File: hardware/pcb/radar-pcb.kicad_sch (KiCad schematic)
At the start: 49 parts, among them J1 DC 5,5x2,5 mm (+ w srodku), J2 DevKit J1, J3 DevKit J3, J4 HC-SR04 (kabel): VCC TRIG ECH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, J5 Serwo SG90 (kabel): GND +5V S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, J6 MAX7219 Elegoo: VCC GND DIN C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, J7 OLED SH1106: VCC GND SCK SDA, J8 Buzzer: + -, J9 Przycisk zewnetrzny, Q1 AO3401A (P-MOSFET), Q2 MMBT3904, SW1 Przycisk ON/standby (katowy), U1 SN74AHCT125N

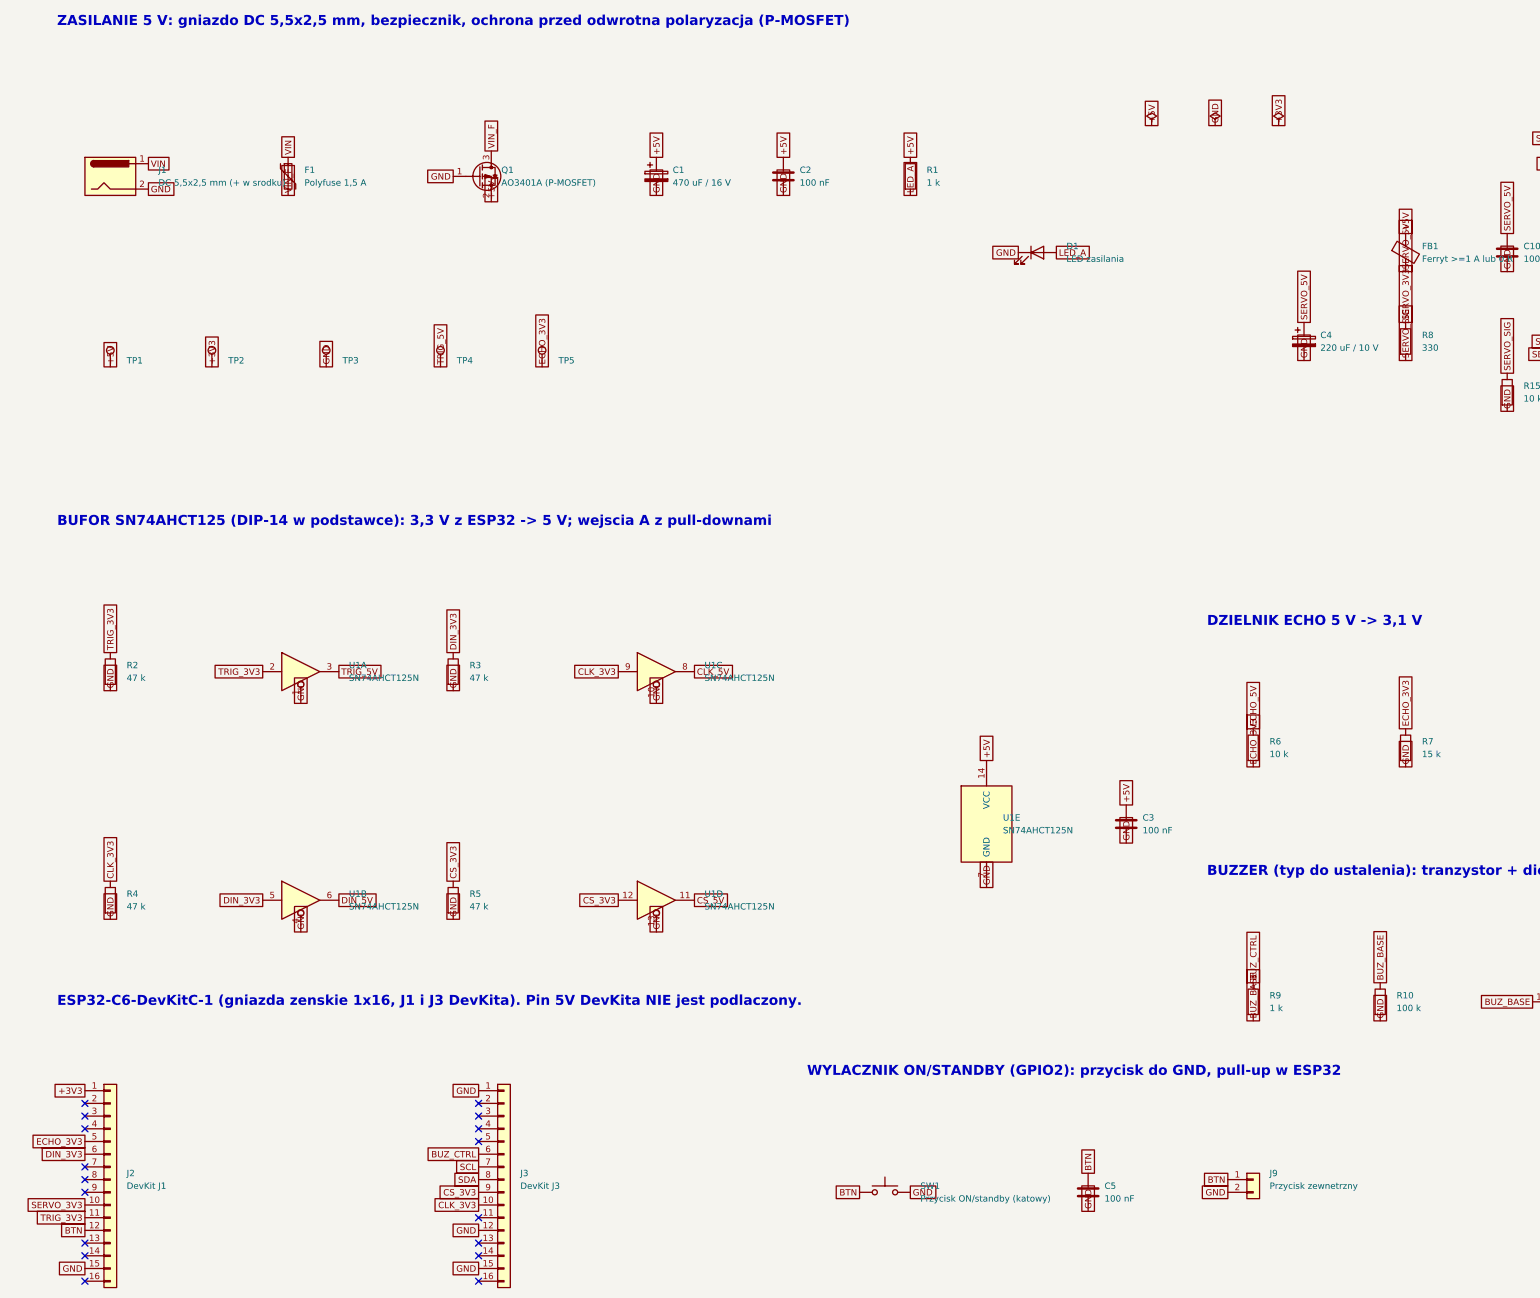
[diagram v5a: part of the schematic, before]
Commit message: PCB: USB-C power input replaces DC jack; DevKit 5V pin tied to board 5V
Co-Authored-By: Claude Sonnet 5.5 <noreply@anthropic.com>
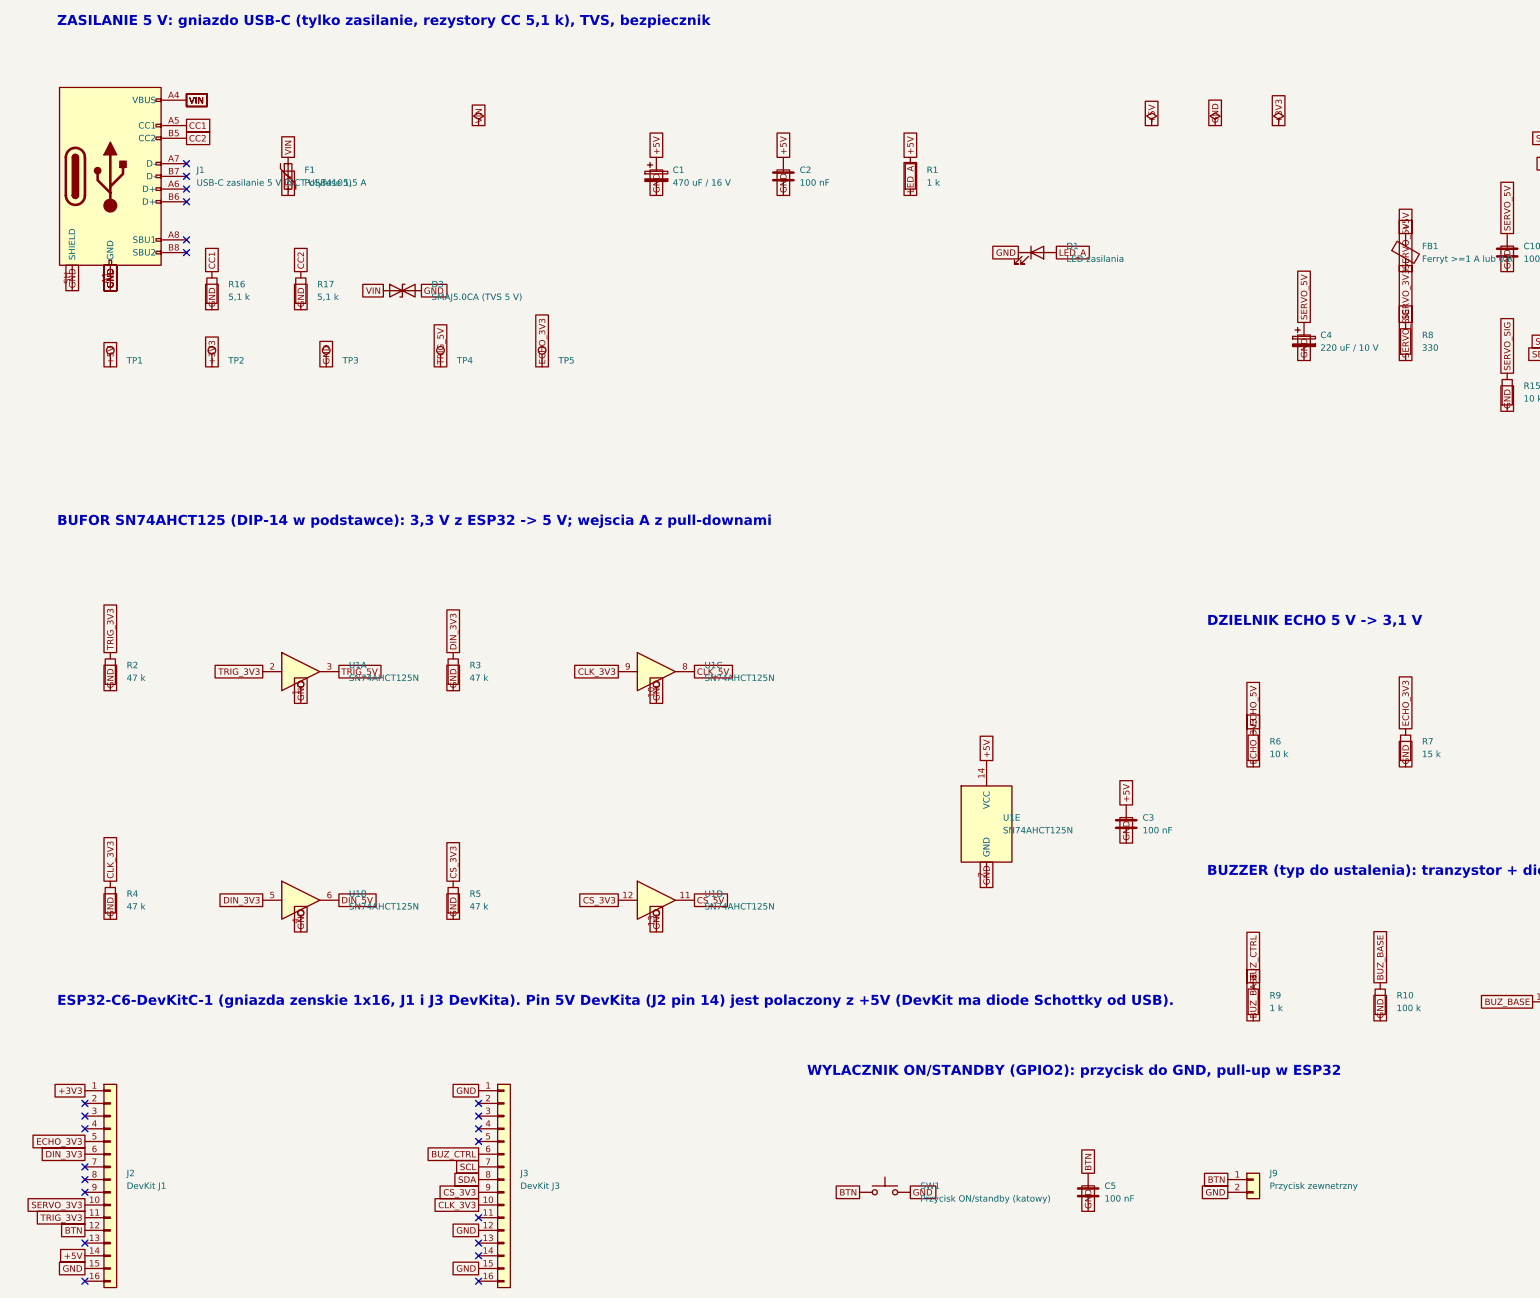
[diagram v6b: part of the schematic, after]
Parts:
- removed J1: DC 5,5x2,5 mm (+ w srodku), Connector_BarrelJack:BarrelJack_Horizontal, symbol Connector:Barrel_Jack
- removed Q1: AO3401A (P-MOSFET), Package_TO_SOT_SMD:SOT-23, symbol Transistor_FET:AO3401A
- added D3: SMAJ5.0CA (TVS 5 V), Diode_SMD:D_SMA, symbol Device:D_TVS
- added J1: USB-C zasilanie 5 V (GCT USB4105), Connector_USB:USB_C_Receptacle_GCT_USB4105-xx-A_16P_TopMnt_Horizontal, symbol Connector:USB_C_Receptacle_USB2.0_16P
- added R16, R17: 5,1 k, Resistor_SMD:R_0805_2012Metric, symbol Device:R
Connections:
- net VIN_F is gone; now on net +5V: F1.2
- net +5V: now also J2.14 (Pin_14)
- net GND: now also D3.2 (A2), J1.A1 (GND), J1.A12 (GND), J1.B1 (GND), J1.B12 (GND), J1.SH (SHIELD), R16.2, R17.2
- net VIN: now also D3.1 (A1), J1.A4 (VBUS), J1.A9 (VBUS), J1.B4 (VBUS), J1.B9 (VBUS)
- new net CC1: J1.A5 (CC1), R16.1
- new net CC2: J1.B5 (CC2), R17.1
- no-connect marks 17 -> 22
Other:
- note added: "ESP32-C6-DevKitC-1 (gniazda zenskie 1x16, J1 i J3 DevKita). Pin 5V DevKita (J2 pin 14) jest polaczony z +5V (DevKit ma diode Schottky od USB)."
- note added: "ZASILANIE 5 V: gniazdo USB-C (tylko zasilanie, rezystory CC 5,1 k), TVS, bezpiecznik"
- note removed: "ESP32-C6-DevKitC-1 (gniazda zenskie 1x16, J1 i J3 DevKita). Pin 5V DevKita NIE jest podlaczony."
- note removed: "ZASILANIE 5 V: gniazdo DC 5,5x2,5 mm, bezpiecznik, ochrona przed odwrotna polaryzacja (P-MOSFET)"

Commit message: PCB: apply audit findings (load switch, D4, SOIC buffer, CS pull-up, antenna keepout, ADC sense), clean silkscreen
Co-Authored-By: Claude Sonnet 5.5 <noreply@anthropic.com>
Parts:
- removed D3: SMAJ5.0CA (TVS 5 V), Diode_SMD:D_SMA, symbol Device:D_TVS
- removed F1: Polyfuse 1,5 A, Fuse:Fuse_1812_4532Metric, symbol Device:Polyfuse
- added C13, C14, C15: 100 nF, Capacitor_SMD:C_0805_2012Metric, symbol Device:C
- added C16: 1 uF, Capacitor_SMD:C_0805_2012Metric, symbol Device:C
- added D3: SMAJ5.0A (TVS 5 V, jednokierunkowy), Diode_SMD:D_SMA, symbol Device:D_Zener
- added D4: 1N5819HW, Diode_SMD:D_SOD-123, symbol Device:D_Schottky
- added J10: Awaryjne wgrywanie: RST GND BOOT (zwarcie sasiedn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, Connector_PinHeader_2.54mm:PinHeader_1x03_P2.54mm_Vertical, symbol Connector_Generic:Conn_01x03
- added R18: 1 k, Resistor_SMD:R_0805_2012Metric, symbol Device:R
- added R19: 10 k, Resistor_SMD:R_0805_2012Metric, symbol Device:R
- added R20, R22, R23: 100 k, Resistor_SMD:R_0805_2012Metric, symbol Device:R
- added R21: 47 k, Resistor_SMD:R_0805_2012Metric, symbol Device:R
- added R24, R25: 4,7 k (nie montowac), Resistor_SMD:R_0805_2012Metric, symbol Device:R
- added TP6: TP SERVO_5V, TestPoint:TestPoint_Pad_D1.5mm, symbol Connector:TestPoint
- added U2: AP22804AW5 (przelacznik 5 V, limit ok. 2,5-3 A), Package_TO_SOT_SMD:SOT-23-5, symbol Power_Management:AP22804AW5
- FB1: value Ferryt >=1 A lub 0 R -> 0 R (zworka; opcja: ferryt >= 1 A)
- U1: value SN74AHCT125N -> SN74AHCT125D; footprint Package_DIP:DIP-14_W7.62mm_Socket -> Package_SO:SOIC-14_3.9x8.7mm_P1.27mm
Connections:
- net +3V3: now also R5.2, R19.2, R24.2, R25.2
- net +5V: now also D4.2 (A), R20.1, U2.1 (OUT); no longer J2.14 (Pin_14)
- net BTN: now also R18.1, R19.1; no longer C5.1, J2.12 (Pin_12)
- net CC1: now also R22.1
- net CC2: now also R23.1
- net GND: now also C13.2, C14.2, C15.2, C16.2, D3.2 (A), J10.2 (Pin_2), R21.2, U2.2 (GND); no longer R5.2
- net SCL: now also R24.1
- net SDA: now also R25.1
- net SERVO_5V: now also TP6.1
- net VIN: now also C16.1, D3.1 (K), U2.4 (EN), U2.5 (IN)
- net CC2_SENSE: now reaches J2.13 (Pin_13)
- net CC2_SENSE: now also C15.1, R23.2
- net EN: now reaches J2.2 (Pin_2)
- net EN: now also J10.1 (Pin_1)
- net V5_SENSE: now reaches J2.7 (Pin_7)
- net V5_SENSE: now also C13.1, R20.2, R21.1
- net CC1_SENSE: now reaches J2.8 (Pin_8)
- net CC1_SENSE: now also C14.1, R22.2
- net BOOT: now reaches J3.11 (Pin_11)
- net BOOT: now also J10.3 (Pin_3)
- new net BTN_ESP: C5.1, J2.12 (Pin_12), R18.2
- new net DEVKIT_5V: D4.1 (K), J2.14 (Pin_14)
- no-connect marks 22 -> 18
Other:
- note added: "DODATKI: dioda 5V DevKita, pomiary ADC (5V, CC1, CC2), BOOT/RST, pull-upy I2C (opcja)"
- note added: "ESP32-C6-DevKitC-1 (gniazda zenskie 1x16, J1 i J3 DevKita). Pin 5V DevKita (J2 pin 14) zasilany z +5V przez diode Schottky D4 (kierunek plytka -> DevKit): USB DevKita nie zasila plytki."
- note added: "ZASILANIE 5 V: gniazdo USB-C (tylko zasilanie, rezystory CC 5,1 k), TVS, przelacznik z miekkim startem"
- note removed: "ESP32-C6-DevKitC-1 (gniazda zenskie 1x16, J1 i J3 DevKita). Pin 5V DevKita (J2 pin 14) jest polaczony z +5V (DevKit ma diode Schottky od USB)."
- note removed: "ZASILANIE 5 V: gniazdo USB-C (tylko zasilanie, rezystory CC 5,1 k), TVS, bezpiecznik"
